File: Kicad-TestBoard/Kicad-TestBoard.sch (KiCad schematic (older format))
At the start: 34 parts, among them CON1 Power 6V-12V, J1 DB9 RS-232 Female, P1 Power 6V-12V, P2 Debug, P4 Arduino, P5 AVR Programmer, P6 RS-232, Q1 Association, Q2 On_Sleep, Q3 Commissioning, SW1 Reset, SW2 Commissioning, U1 78L05, U2 MAX232

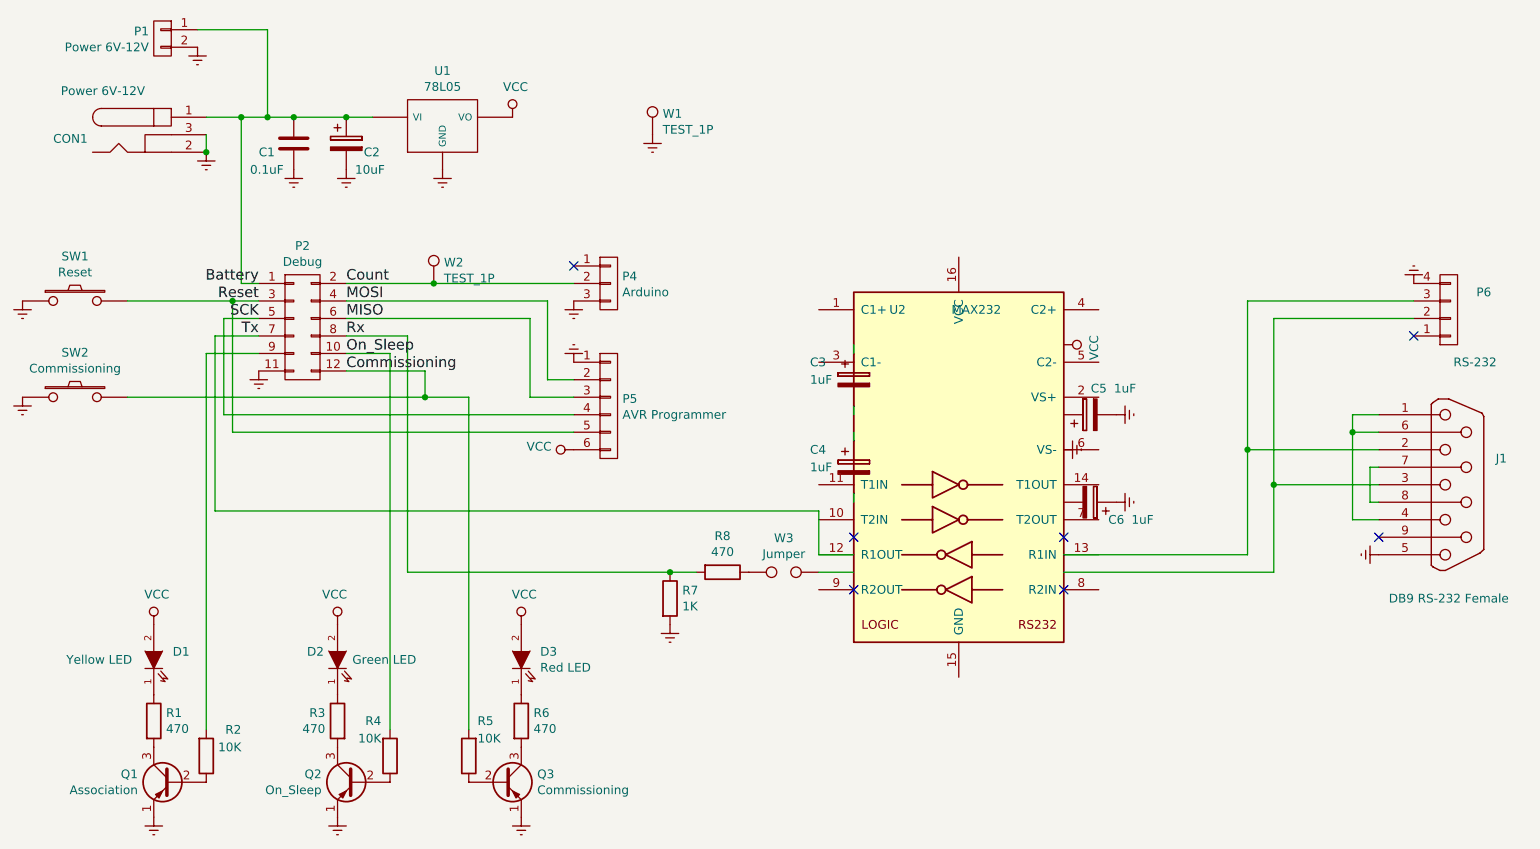
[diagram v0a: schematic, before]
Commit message: Corrections to Testboard PCB. - Incorrect Tx wiring to MAX232 - Make correct allocations of footprints in schematic - Add some extra text including title, version, author, date.
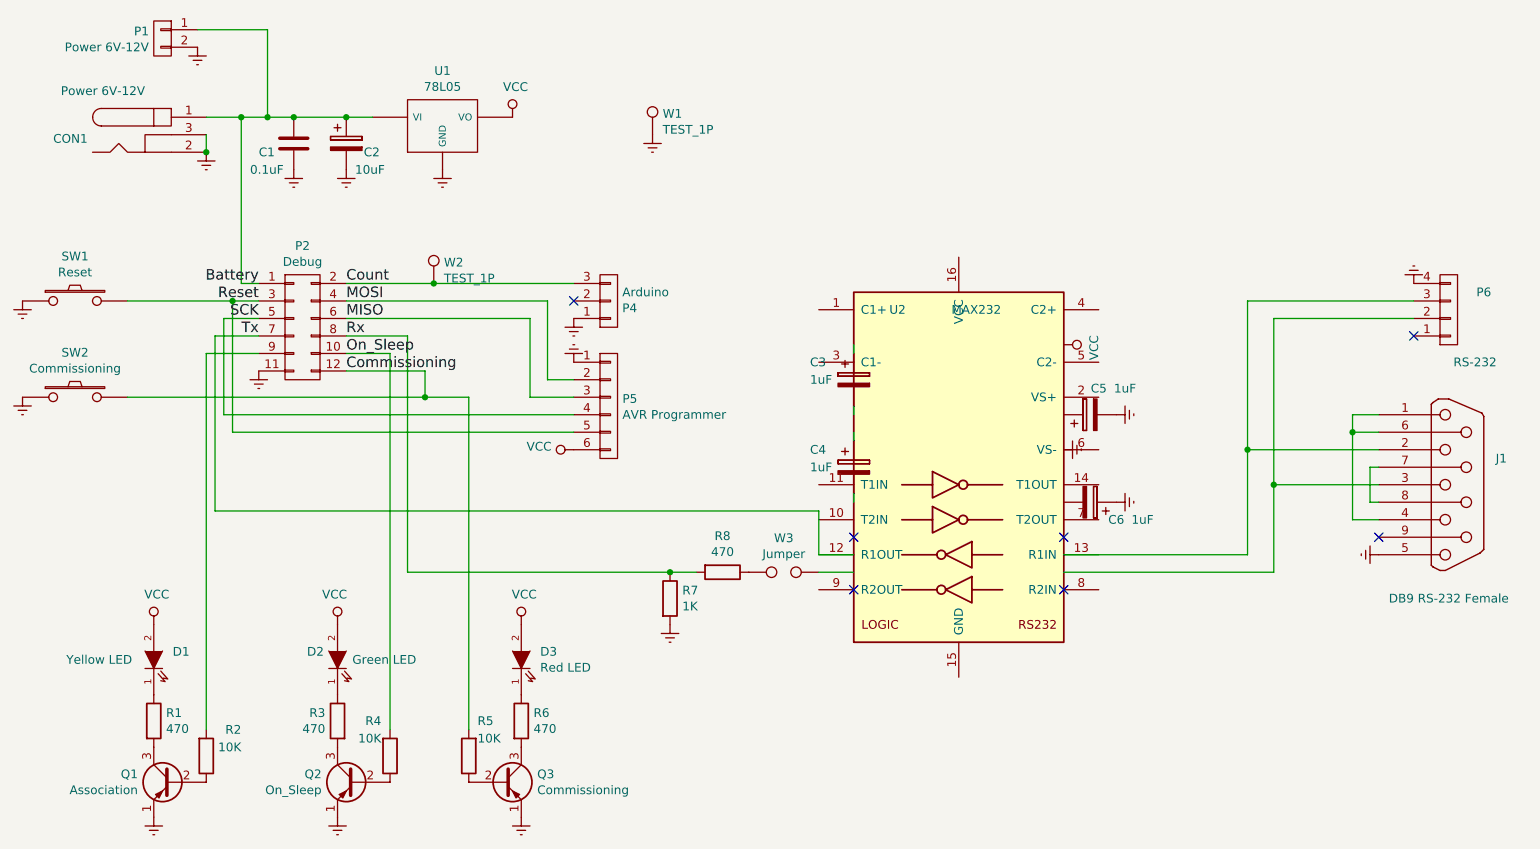
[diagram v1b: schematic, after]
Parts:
- Q1, Q2, Q3: footprint Testboard:TO-92_Molded_Wide -> Testboard:TO-92_Molded_Narrow
- U1: footprint Testboard:TO-92_Molded_Wide -> Testboard:TO-92_78L05
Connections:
- wire segments 66 -> 55
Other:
- moved on the sheet: P4
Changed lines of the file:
@@
 F 0 "U1" H 3400 2715 50  0000 C CNN
 F 1 "78L05" H 3400 2624 50  0000 C CNN
-F 2 "Testboard:TO-92_Molded_Wide" H 3400 2400 50  0001 C CNN
+F 2 "Testboard:TO-92_78L05" H 3400 2400 50  0001 C CNN
 F 3 "" H 3400 2400 50  0000 C CNN
 	1    3400 2400
@@
 L Earth #PWR06
 U 1 1 5757C491
-P 4150 3400
-F 0 "#PWR06" H 4150 3150 50  0001 C CNN
-F 1 "Earth" H 4150 3250 50  0001 C CNN
-F 2 "" H 4150 3400 50  0000 C CNN
-F 3 "" H 4150 3400 50  0000 C CNN
-	1    4150 3400
+P 4150 3500
+F 0 "#PWR06" H 4150 3250 50  0001 C CNN
+F 1 "Earth" H 4150 3350 50  0001 C CNN
+F 2 "" H 4150 3500 50  0000 C CNN
+F 3 "" H 4150 3500 50  0000 C CNN
+	1    4150 3500
 	1    0    0    -1
 $EndComp
@@
 L CONN_01X03 P4
 U 1 1 5757C5D7
-P 4350 3300
-F 0 "P4" H 4427 3341 50  0000 L CNN
-F 1 "Arduino" H 4427 3250 50  0000 L CNN
-F 2 "Testboard:PINHEAD1-3" H 4350 3300 50  0001 C CNN
-F 3 "" H 4350 3300 50  0000 C CNN
-	1    4350 3300
-	1    0    0    -1
+P 4350 3400
+F 0 "P4" H 4427 3441 50  0000 L CNN
+F 1 "Arduino" H 4427 3350 50  0000 L CNN
+F 2 "Testboard:PINHEAD1-3" H 4350 3400 50  0001 C CNN
+F 3 "" H 4350 3400 50  0000 C CNN
+	1    4350 3400
+	1    0    0    1
 $EndComp
 $Comp
@@
 F 0 "Q3" H 3941 6196 50  0000 L CNN
 F 1 "Commissioning" H 3941 6105 50  0000 L CNN
-F 2 "Testboard:TO-92_Molded_Wide" H 3950 6250 50  0001 C CNN
+F 2 "Testboard:TO-92_Molded_Narrow" H 3950 6250 50  0001 C CNN
 F 3 "" H 3750 6150 50  0000 C CNN
 	1    3750 6150
@@
 F 0 "Q2" H 3091 6196 50  0000 L CNN
 F 1 "On_Sleep" H 3091 6105 50  0000 L CNN
-F 2 "Testboard:TO-92_Molded_Wide" H 3100 6250 50  0001 C CNN
+F 2 "Testboard:TO-92_Molded_Narrow" H 3100 6250 50  0001 C CNN
 F 3 "" H 2900 6150 50  0000 C CNN
 	1    2900 6150
@@
 F 0 "Q1" H 2041 6196 50  0000 L CNN
 F 1 "Association" H 2041 6105 50  0000 L CNN
-F 2 "Testboard:TO-92_Molded_Wide" H 2050 6250 50  0001 C CNN
+F 2 "Testboard:TO-92_Molded_Narrow" H 2050 6250 50  0001 C CNN
 F 3 "" H 1850 6150 50  0000 C CNN
 	1    1850 6150
@@
 NoConn ~ 5750 5050
 NoConn ~ 5750 4750
-NoConn ~ 4150 3200
+NoConn ~ 4150 3400
 $Comp
 L Earth #PWR025
@@
 $EndComp
 Wire Wire Line
-	2050 2350 2250 2350
-Wire Wire Line
-	2250 2350 2400 2350
-Wire Wire Line
-	2400 2350 2550 2350
-Wire Wire Line
-	2550 2350 2850 2350
-Wire Wire Line
-	2850 2350 3000 2350
+	2050 2350 3000 2350
 Wire Wire Line
 	2000 1850 2400 1850
@@
 	2050 3700 2050 5850
 Wire Wire Line
-	2850 3300 3350 3300
-Wire Wire Line
-	3350 3300 4150 3300
+	2850 3300 4150 3300
 Wire Wire Line
 	2850 3400 4000 3400
@@
 Connection ~ 2200 3400
 Wire Wire Line
-	1600 3400 2200 3400
-Wire Wire Line
-	2200 3400 2350 3400
-Wire Wire Line
-	1600 3950 3300 3950
-Wire Wire Line
-	3300 3950 3550 3950
+	1600 3400 2350 3400
+Wire Wire Line
+	1600 3950 3550 3950
 Connection ~ 3350 3300
 Wire Wire Line
@@
 Connection ~ 3300 3950
 Wire Wire Line
-	3200 4950 4700 4950
-Wire Wire Line
-	4700 4950 4850 4950
+	3200 4950 4850 4950
 Connection ~ 2850 2350
 Connection ~ 2550 2350
 Wire Wire Line
-	8150 3500 8150 4450
-Wire Wire Line
-	8150 4450 8150 4950
-Wire Wire Line
-	8000 3400 8000 4250
-Wire Wire Line
-	8000 4250 8000 4850
+	8150 3500 8150 4950
+Wire Wire Line
+	8000 3400 8000 4850
 Wire Wire Line
 	8000 3400 8950 3400
@@
 	8750 4050 8600 4050
 Wire Wire Line
-	8600 4050 8600 4150
-Wire Wire Line
-	8600 4150 8600 4650
+	8600 4050 8600 4650
 Wire Wire Line
 	8600 4150 8750 4150

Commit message: Add power jumper to disconnect testboard power from meter when battery is present in the latter.
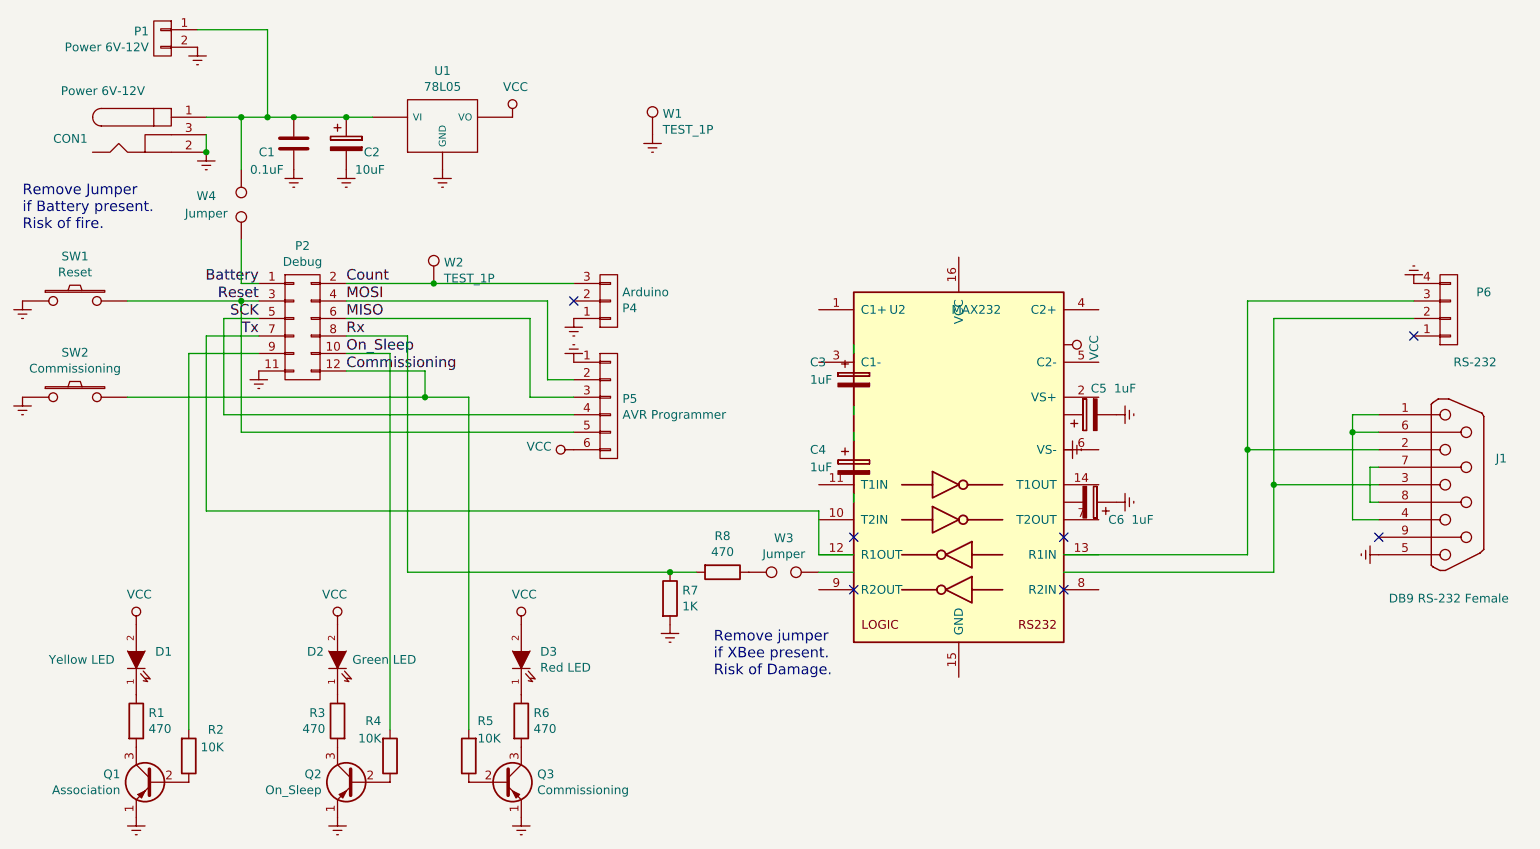
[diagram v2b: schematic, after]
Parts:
- added W4: Jumper, Testboard:SIL-2, symbol TEST
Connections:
- wire segments 55 -> 56
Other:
- note added: "Remove Jumper\nif Battery present.\nRisk of fire."
- note added: "Remove jumper\nif XBee present.\nRisk of Damage."
- moved on the sheet: D1, Q1, R1, R2
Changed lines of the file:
@@
 L LED D1
 U 1 1 575826BC
-P 1750 5450
-F 0 "D1" V 1796 5342 50  0000 R CNN
-F 1 "Yellow LED" V 1750 5950 50  0000 R CNN
-F 2 "Testboard:LED-5MM" H 1750 5450 50  0001 C CNN
-F 3 "" H 1750 5450 50  0000 C CNN
-	1    1750 5450
+P 1650 5450
+F 0 "D1" V 1696 5342 50  0000 R CNN
+F 1 "Yellow LED" V 1650 5950 50  0000 R CNN
+F 2 "Testboard:LED-5MM" H 1650 5450 50  0001 C CNN
+F 3 "" H 1650 5450 50  0000 C CNN
+	1    1650 5450
 	0    -1   -1   0
 $EndComp
@@
 L VCC #PWR015
 U 1 1 57582756
-P 1750 5250
-F 0 "#PWR015" H 1750 5100 50  0001 C CNN
-F 1 "VCC" H 1767 5423 50  0000 C CNN
-F 2 "" H 1750 5250 50  0000 C CNN
-F 3 "" H 1750 5250 50  0000 C CNN
-	1    1750 5250
+P 1650 5250
+F 0 "#PWR015" H 1650 5100 50  0001 C CNN
+F 1 "VCC" H 1667 5423 50  0000 C CNN
+F 2 "" H 1650 5250 50  0000 C CNN
+F 3 "" H 1650 5250 50  0000 C CNN
+	1    1650 5250
 	1    0    0    -1
 $EndComp
@@
 L R R1
 U 1 1 575827A9
-P 1750 5800
-F 0 "R1" H 1820 5846 50  0000 L CNN
-F 1 "470" H 1820 5755 50  0000 L CNN
-F 2 "Testboard:Resistor_Horizontal_RM10mm" V 1680 5800 50  0001 C CNN
-F 3 "" H 1750 5800 50  0000 C CNN
-	1    1750 5800
+P 1650 5800
+F 0 "R1" H 1720 5846 50  0000 L CNN
+F 1 "470" H 1720 5755 50  0000 L CNN
+F 2 "Testboard:Resistor_Horizontal_RM10mm" V 1580 5800 50  0001 C CNN
+F 3 "" H 1650 5800 50  0000 C CNN
+	1    1650 5800
 	1    0    0    -1
 $EndComp
@@
 L Q_PNP_EBC Q1
 U 1 1 575828F8
-P 1850 6150
-F 0 "Q1" H 2041 6196 50  0000 L CNN
-F 1 "Association" H 2041 6105 50  0000 L CNN
-F 2 "Testboard:TO-92_Molded_Narrow" H 2050 6250 50  0001 C CNN
-F 3 "" H 1850 6150 50  0000 C CNN
-	1    1850 6150
+P 1750 6150
+F 0 "Q1" H 1941 6196 50  0000 L CNN
+F 1 "Association" H 1941 6105 50  0000 L CNN
+F 2 "Testboard:TO-92_Molded_Narrow" H 1950 6250 50  0001 C CNN
+F 3 "" H 1750 6150 50  0000 C CNN
+	1    1750 6150
 	-1   0    0    -1
 $EndComp
@@
 L R R2
 U 1 1 57582990
-P 2050 6000
-F 0 "R2" H 2250 5850 50  0000 R CNN
-F 1 "10K" H 2250 5950 50  0000 R CNN
-F 2 "Testboard:Resistor_Horizontal_RM10mm" V 1980 6000 50  0001 C CNN
-F 3 "" H 2050 6000 50  0000 C CNN
-	1    2050 6000
+P 1950 6000
+F 0 "R2" H 2150 5850 50  0000 R CNN
+F 1 "10K" H 2150 5950 50  0000 R CNN
+F 2 "Testboard:Resistor_Horizontal_RM10mm" V 1880 6000 50  0001 C CNN
+F 3 "" H 1950 6000 50  0000 C CNN
+	1    1950 6000
 	1    0    0    1
 $EndComp
@@
 L Earth #PWR016
 U 1 1 57582A1D
-P 1750 6350
-F 0 "#PWR016" H 1750 6100 50  0001 C CNN
-F 1 "Earth" H 1750 6200 50  0001 C CNN
-F 2 "" H 1750 6350 50  0000 C CNN
-F 3 "" H 1750 6350 50  0000 C CNN
-	1    1750 6350
+P 1650 6350
+F 0 "#PWR016" H 1650 6100 50  0001 C CNN
+F 1 "Earth" H 1650 6200 50  0001 C CNN
+F 2 "" H 1650 6350 50  0000 C CNN
+F 3 "" H 1650 6350 50  0000 C CNN
+	1    1650 6350
 	-1   0    0    -1
 $EndComp
@@
 	2350 3300 2250 3300
 Wire Wire Line
-	2250 3300 2250 2350
-Wire Wire Line
-	2200 3400 2200 4150
+	2250 3400 2250 4150
 Wire Wire Line
 	2350 3500 2150 3500
@@
 	2150 3500 2150 4050
 Wire Wire Line
-	2350 3600 2100 3600
-Wire Wire Line
-	2100 3600 2100 4600
-Wire Wire Line
-	2050 3700 2050 5850
+	2350 3600 2050 3600
+Wire Wire Line
+	2050 3600 2050 4600
+Wire Wire Line
+	1950 3700 1950 5850
 Wire Wire Line
 	2850 3300 4150 3300
@@
 Wire Wire Line
 	3550 3950 3550 5850
-Connection ~ 2200 3400
+Connection ~ 2250 3400
 Wire Wire Line
 	1600 3400 2350 3400
@@
 	2150 4050 4150 4050
 Wire Wire Line
-	2200 4150 4150 4150
-Wire Wire Line
-	2100 4600 5550 4600
+	2250 4150 4150 4150
+Wire Wire Line
+	2050 4600 5550 4600
 Connection ~ 3300 3950
 Wire Wire Line
@@
 Connection ~ 4700 4950
 Wire Wire Line
-	2050 3700 2350 3700
+	1950 3700 2350 3700
 Wire Wire Line
 	2050 2450 2050 2550
@@
 Wire Wire Line
 	5550 4950 5750 4950
+$Comp
+L TEST W4
+U 1 1 586F1BEF
+P 2250 2850
+F 0 "W4" V 2300 3050 50  0000 C CNN
+F 1 "Jumper" V 2200 3050 50  0000 C CNN
+F 2 "Testboard:SIL-2" H 2250 2850 50  0001 C CNN
+F 3 "" H 2250 2850 50  0000 C CNN
+	1    2250 2850
+	0    -1   -1   0
+$EndComp
+Wire Wire Line
+	2250 2350 2250 2650
+Wire Wire Line
+	2250 3300 2250 3050
+Text Notes 4950 5550 0    60   ~ 0
+Remove jumper\nif XBee present.\nRisk of Damage.
+Text Notes 1000 3000 0    60   ~ 0
+Remove Jumper\nif Battery present.\nRisk of fire.
 $EndSCHEMATC

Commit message: Kicad-Main, Kicad-Mounts and Kicad-Testboard. Add a range of symbol and footprint libraries and repair some problems apparently due to randomized changes in Kicad repository libraries.
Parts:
- removed D1: Yellow LED, Testboard:LED-5MM, symbol LED
- removed D2: Green LED, Testboard:LED-5MM, symbol LED
- removed D3: Red LED, Testboard:LED-5MM, symbol LED
- removed W3, W4: Jumper, Testboard:SIL-2, symbol TEST
- added D1: Yellow LED, Testboard:LED-5MM, symbol LED_ALT
- added D2: Green LED, Testboard:LED-5MM, symbol LED_ALT
- added D3: Red LED, Testboard:LED-5MM, symbol LED_ALT
- added JP1: Power Jumper, Testboard:SIL-1, symbol Jumper_NO_Small
- added JP2: Tx Jumper, Testboard:SIL-1, symbol Jumper_NO_Small
- renumbered P4 to P3, P5 to P4, P6 to P5, W2 to W1, W1 to W2
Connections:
- wire segments 56 -> 49
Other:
- moved on the sheet: C3, C4, C5, C6, J1, P5, R7, R8, U2
